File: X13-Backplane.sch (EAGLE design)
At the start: 24 parts, among them J1 284512-4, J2 284512-4, J3 284512-8, J4 284512-8, J5 284512-4, T1 284512-3, T2 284512-3, T3 284512-3, T4 284512-3, T5 284512-3, T6 284512-3, T7 284512-3, T8 284512-3

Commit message: updated schematic
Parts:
- removed R2: 10k, SparkFun-Resistors:10KOHM-0603-1/10W-1%
- removed R3: 4.7k, SparkFun-Resistors:1KOHM-0603-1/10W-1%
- removed U$7, U$8: ESC2BACKPLANE, ESC_to_Backplane_Connectors:ESC2BACKPLANE
- added DIST_LOGIC_TO_BACKPLANE: IPL1-107-01-L-D-RE-P, Backplane_Dist_Logic_Connector:IPL1-107-01-L-D-RE-P
- added DIST_TO_BACKPLANE: (no value), Samtec MPPT Hermaphoditic 10 pos - MPPT-10-01-01-L-RA-SD:MPPT-10-01-01-L-RA-SD
- added J8: 284512-8, 284512-8:284512-8
- added R4: 22k, SparkFun-Resistors:26.7KOHM0603-1/10W-1%
- added R5: 4.7k, SparkFun-Resistors:1KOHM-0603-1/10W-1%
- added SOLENOID_CONNECTOR: SAMTEC-CLT-111-01-X-DJ, Solenoid Connector - SAMTEC-CLT-111-01-X-D:SAMTEC-CLT-111-01-X-DJ
- added U$1, U$2: BACKPLANE_CONNECTORS, BLHeli_32 45A:BACKPLANE_CONNECTORS
- R1: value 22k -> 10k; device SparkFun-Resistors:26.7KOHM0603-1/10W-1% -> SparkFun-Resistors:10KOHM-0603-1/10W-1%
- U$3: value ESC2BACKPLANE -> BACKPLANE_CONNECTORS; device ESC_to_Backplane_Connectors:ESC2BACKPLANE -> BLHeli_32 45A:BACKPLANE_CONNECTORS
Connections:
- removed net ESC-ID_1: R1.2, U$3G$1.P$8
- removed net ESC-ID_2: R2.2, U$7G$1.P$8
- removed net ESC-ID_3: R3.2, U$8G$1.P$8
- new net ALERT_1: DIST_LOGIC_TO_BACKPLANE.11, SOLENOID_CONNECTOR.18
- new net ALERT_2: DIST_LOGIC_TO_BACKPLANE.10, SOLENOID_CONNECTOR.17
- new net C2_1: DIST_LOGIC_TO_BACKPLANE.8, SOLENOID_CONNECTOR.16
- new net C2_2: DIST_LOGIC_TO_BACKPLANE.7, SOLENOID_CONNECTOR.15
- new net CLK: DIST_LOGIC_TO_BACKPLANE.9, SOLENOID_CONNECTOR.20
- new net DATA: DIST_LOGIC_TO_BACKPLANE.12, SOLENOID_CONNECTOR.22
- new net ESCID_1: R4.2, U$1G$3.12
- new net ESCID_2: R1.2, U$2G$3.12
- new net ESCID_3: R5.2, U$3G$3.12
- new net SOL1_1: J8.1, SOLENOID_CONNECTOR.2
- new net SOL2_1: J8.2, SOLENOID_CONNECTOR.1
- new net SOL3_1: J8.3, SOLENOID_CONNECTOR.3
- new net SOL4_1: J8.4, SOLENOID_CONNECTOR.5
- new net SOL5_1: J8.5, SOLENOID_CONNECTOR.7
- new net SOL6_1: J8.6, SOLENOID_CONNECTOR.9
- net 12V: now also DIST_TO_BACKPLANE.10, DIST_TO_BACKPLANE.6, DIST_TO_BACKPLANE.7, DIST_TO_BACKPLANE.8, DIST_TO_BACKPLANE.9, SOLENOID_CONNECTOR.11, U$1G$1.1, U$1G$1.2, U$1G$1.3, U$1G$1.4, U$1G$1.5, U$1G$1.6, U$1G$1.7, U$1G$1.8, U$1G$2.1, U$1G$2.2, U$1G$2.3, U$1G$2.4, U$1G$2.5, U$1G$2.6, U$1G$2.7, U$1G$2.8, U$2G$1.1, U$2G$1.2, U$2G$1.3, U$2G$1.4, U$2G$1.5, U$2G$1.6, U$2G$1.7, U$2G$1.8, U$2G$2.1, U$2G$2.2, U$2G$2.3, U$2G$2.4, U$2G$2.5, U$2G$2.6, U$2G$2.7, U$2G$2.8, U$3G$1.1, U$3G$1.2, U$3G$1.3, U$3G$1.4, U$3G$1.5, U$3G$1.6, U$3G$1.7, U$3G$1.8, U$3G$2.1, U$3G$2.2, U$3G$2.3, U$3G$2.4, U$3G$2.5, U$3G$2.6, U$3G$2.7, U$3G$2.8; no longer U$3G$1.P$10, U$3G$1.P$11, U$3G$1.P$12, U$3G$1.P$13, U$3G$1.P$23, U$3G$1.P$24, U$3G$1.P$25, U$3G$1.P$26, U$3G$1.P$27, U$3G$1.P$9, U$3G$2.P$A, U$3G$2.P$B, U$3G$2.P$C, U$3G$2.P$D, U$3G$2.P$E, U$3G$2.P$O, U$3G$2.P$P, U$3G$2.P$Q, U$3G$2.P$R, U$3G$2.P$S, U$7G$1.P$10, U$7G$1.P$11, U$7G$1.P$12, U$7G$1.P$13, U$7G$1.P$23, U$7G$1.P$24, U$7G$1.P$25, U$7G$1.P$26, U$7G$1.P$27, U$7G$1.P$9, U$7G$2.P$A, U$7G$2.P$B, U$7G$2.P$C, U$7G$2.P$D, U$7G$2.P$E, U$7G$2.P$O, U$7G$2.P$P, U$7G$2.P$Q, U$7G$2.P$R, U$7G$2.P$S, U$8G$1.P$10, U$8G$1.P$11, U$8G$1.P$12, U$8G$1.P$13, U$8G$1.P$23, U$8G$1.P$24, U$8G$1.P$25, U$8G$1.P$26, U$8G$1.P$27, U$8G$1.P$9, U$8G$2.P$A, U$8G$2.P$B, U$8G$2.P$C, U$8G$2.P$D, U$8G$2.P$E, U$8G$2.P$O, U$8G$2.P$P, U$8G$2.P$Q, U$8G$2.P$R, U$8G$2.P$S
- net 3.3V: now also DIST_LOGIC_TO_BACKPLANE.4, SOLENOID_CONNECTOR.6, U$1G$3.1, U$1G$3.2, U$1G$3.3, U$1G$3.4, U$2G$3.1, U$2G$3.2, U$2G$3.3, U$2G$3.4, U$3G$3.1, U$3G$3.2, U$3G$3.3, U$3G$3.4; no longer U$3G$2.P$G, U$3G$2.P$H, U$3G$2.P$U, U$3G$2.P$V, U$7G$2.P$G, U$7G$2.P$H, U$7G$2.P$U, U$7G$2.P$V, U$8G$2.P$G, U$8G$2.P$H, U$8G$2.P$U, U$8G$2.P$V
- net 5V: now also DIST_LOGIC_TO_BACKPLANE.1, DIST_LOGIC_TO_BACKPLANE.2, DIST_LOGIC_TO_BACKPLANE.3
- net CAN_H: now also SOLENOID_CONNECTOR.19, U$1G$3.5, U$2G$3.5, U$3G$3.5; no longer U$3G$1.P$6, U$7G$1.P$6, U$8G$1.P$6
- net CAN_L: now also SOLENOID_CONNECTOR.21, U$1G$3.7, U$2G$3.7, U$3G$3.7; no longer U$3G$1.P$7, U$7G$1.P$7, U$8G$1.P$7
- net GND: now also DIST_LOGIC_TO_BACKPLANE.5, DIST_LOGIC_TO_BACKPLANE.6, DIST_TO_BACKPLANE.1, DIST_TO_BACKPLANE.2, DIST_TO_BACKPLANE.3, DIST_TO_BACKPLANE.4, DIST_TO_BACKPLANE.5, R4.1, R5.1, SOLENOID_CONNECTOR.10, SOLENOID_CONNECTOR.12, SOLENOID_CONNECTOR.4, SOLENOID_CONNECTOR.8, U$1G$1.10, U$1G$1.11, U$1G$1.12, U$1G$1.9, U$1G$2.10, U$1G$2.11, U$1G$2.12, U$1G$2.9, U$2G$1.10, U$2G$1.11, U$2G$1.12, U$2G$1.9, U$2G$2.10, U$2G$2.11, U$2G$2.12, U$2G$2.9, U$3G$1.10, U$3G$1.11, U$3G$1.12, U$3G$1.9, U$3G$2.10, U$3G$2.11, U$3G$2.12, U$3G$2.9; no longer R2.1, R3.1, U$3G$1.P$1, U$3G$1.P$15, U$3G$1.P$16, U$3G$1.P$17, U$3G$1.P$18, U$3G$1.P$2, U$3G$1.P$3, U$3G$1.P$4, U$3G$2.P$AA, U$3G$2.P$BB, U$3G$2.P$J, U$3G$2.P$K, U$3G$2.P$L, U$3G$2.P$M, U$3G$2.P$N, U$3G$2.P$X, U$3G$2.P$Y, U$3G$2.P$Z, U$7G$1.P$1, U$7G$1.P$15, U$7G$1.P$16, U$7G$1.P$17, U$7G$1.P$18, U$7G$1.P$2, U$7G$1.P$3, U$7G$1.P$4, U$7G$2.P$AA, U$7G$2.P$BB, U$7G$2.P$J, U$7G$2.P$K, U$7G$2.P$L, U$7G$2.P$M, U$7G$2.P$N, U$7G$2.P$X, U$7G$2.P$Y, U$7G$2.P$Z, U$8G$1.P$1, U$8G$1.P$15, U$8G$1.P$16, U$8G$1.P$17, U$8G$1.P$18, U$8G$1.P$2, U$8G$1.P$3, U$8G$1.P$4, U$8G$2.P$AA, U$8G$2.P$BB, U$8G$2.P$J, U$8G$2.P$K, U$8G$2.P$L, U$8G$2.P$M, U$8G$2.P$N, U$8G$2.P$X, U$8G$2.P$Y, U$8G$2.P$Z
- net NRST: now also U$1G$3.6, U$2G$3.6, U$3G$3.6; no longer U$3G$1.P$20, U$7G$1.P$20, U$8G$1.P$20
- net PROG_1: now also U$1G$3.8; no longer U$3G$1.P$5
- net PROG_2: now also U$2G$3.8; no longer U$7G$1.P$5
- net PROG_3: now also U$3G$3.8; no longer U$8G$1.P$5
- net SWCLK_1: now also U$1G$3.11; no longer U$3G$1.P$22
- net SWCLK_2: now also U$2G$3.11; no longer U$7G$1.P$22
- net SWCLK_3: now also U$3G$3.11; no longer U$8G$1.P$22
- net SWDIO_1: now also U$1G$3.9; no longer U$3G$1.P$21
- net SWDIO_2: now also U$2G$3.9; no longer U$7G$1.P$21
- net SWDIO_3: now also U$3G$3.9; no longer U$8G$1.P$21
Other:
- note added: "Solenoid"
- moved on the sheet: MUX, R1

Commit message: wired board
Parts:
- added C1, C2, C3: 10nF, SparkFun-Capacitors:10NF-0603-50V-10%
- added H1, H2, H3: 6-32-HOLE, Mounting Holes:6-32-HOLE
- added J6: 284512-4, 284512-4:284512-4
- added R2, R3, R6: 10k, SparkFun-Resistors:10KOHM-0603-1/10W-1%
- J1, J5: value 284512-4 -> PXC-PTSM-04-RA-1778641; device 284512-4:284512-4 -> Phoenix Contact PTSM-04-V-1778573:PXC-PTSM-04-RA-1778641
- J4: value 284512-8 -> PXC-PTSM-04-RA-1778641; device 284512-8:284512-8 -> Phoenix Contact PTSM-04-V-1778573:PXC-PTSM-04-RA-1778641
- SOLENOID_CONNECTOR: value SAMTEC-CLT-111-01-X-DJ -> TMM-111-01-T-D; device Solenoid Connector - SAMTEC-CLT-111-01-X-D:SAMTEC-CLT-111-01-X-DJ -> Samtec low profile male headers - TMM-111-01-T-D:TMM-111-01-T-D
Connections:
- new net SHIELD_1: C1.1, J1.4, R2.2
- new net SHIELD_2: C2.1, J4.4, R3.2
- new net SHIELD_3: C3.1, J5.4, R6.2
- net 12V: no longer J5.1, J5.2
- net 5V: now also J5.1, J5.2, J6.1; no longer J4.3
- net CAN_H: now also J6.2; no longer J4.4
- net CAN_L: now also J6.3; no longer J4.5
- net GND: now also C1.2, C2.2, C3.2, J4.3, J6.4, J8.7, J8.8, R2.1, R3.1, R6.1; no longer J1.4, J4.6, J4.7, J4.8, J5.4
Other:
- note removed: "Fan"
- moved on the sheet: J1, J2, J5

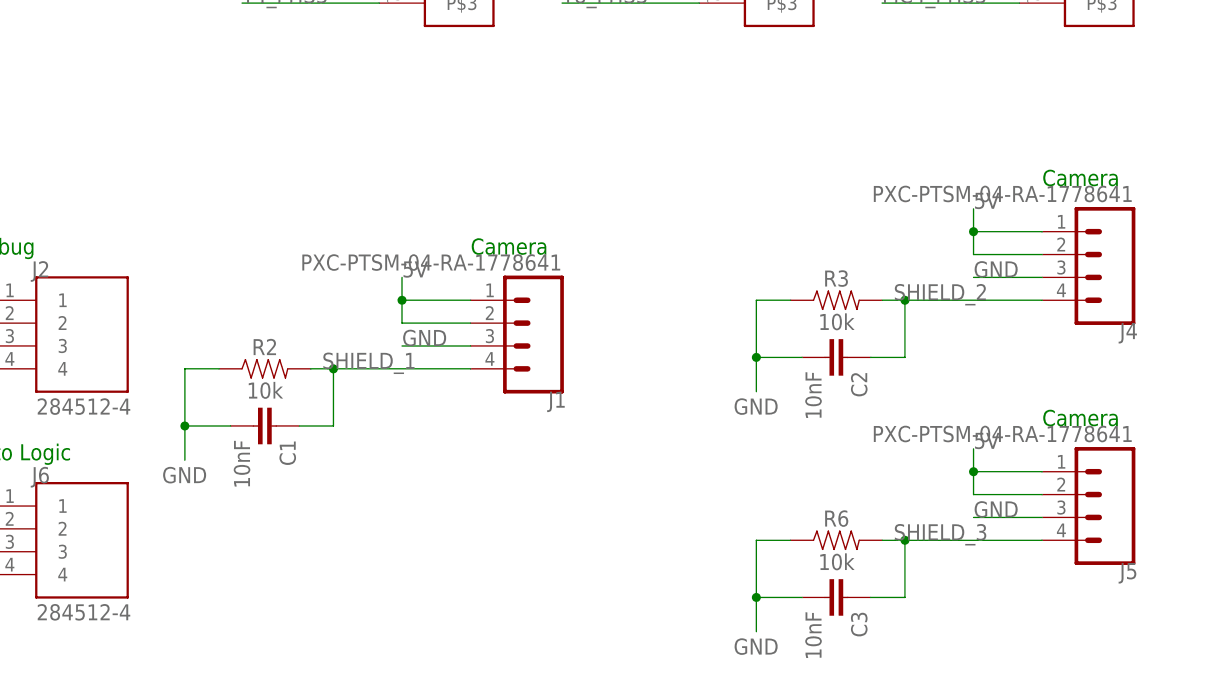
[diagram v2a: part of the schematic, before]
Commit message: updated solenoid connector
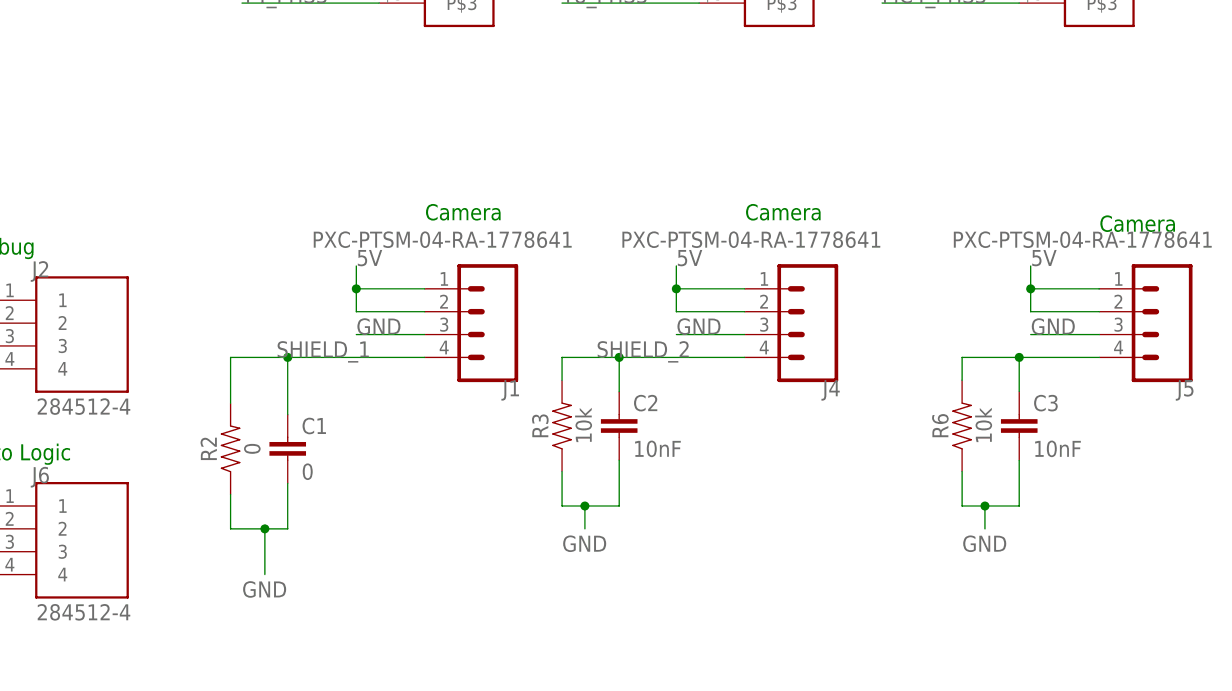
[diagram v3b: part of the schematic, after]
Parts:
- C1: value 10nF -> 0
- R2: value 10k -> 0
- SOLENOID_CONNECTOR: value TMM-111-01-T-D -> BKP-TO-SOL; device Samtec low profile male headers - TMM-111-01-T-D:TMM-111-01-T-D -> Solenoid Connector (backplane side):BKP-TO-SOL
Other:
- moved on the sheet: C1, C2, C3, J1, J4, J5, R2, R3, R6

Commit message: updated mux
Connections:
- removed net SWCLK_4: MUX.1Y3
- removed net SWDIO_4: MUX.2Y3
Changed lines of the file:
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@@
 <setting verticaltext="up"/>
 </settings>
-<grid distance="0.05" unitdist="inch" unit="inch" style="lines" multiple="1" display="no" altdistance="0.01" altunitdist="inch" altunit="inch"/>
+<grid distance="0.1" unitdist="inch" unit="inch" style="lines" multiple="1" display="no" altdistance="0.01" altunitdist="inch" altunit="inch"/>
 <layers>
 <layer number="1" name="Top" color="4" fill="1" visible="no" active="no"/>
@@
 </segment>
 </net>
-<net name="SWDIO_4" class="0">
-<segment>
-<pinref part="MUX" gate="G$1" pin="2Y3"/>
-<wire x1="-96.52" y1="77.47" x2="-106.68" y2="77.47" width="0.1524" layer="91"/>
-<label x="-106.68" y="77.47" size="1.778" layer="95"/>
-</segment>
-</net>
-<net name="SWCLK_4" class="0">
-<segment>
-<pinref part="MUX" gate="G$1" pin="1Y3"/>
-<wire x1="-68.58" y1="72.39" x2="-58.42" y2="72.39" width="0.1524" layer="91"/>
-<label x="-68.58" y="72.39" size="1.778" layer="95"/>
-</segment>
-</net>

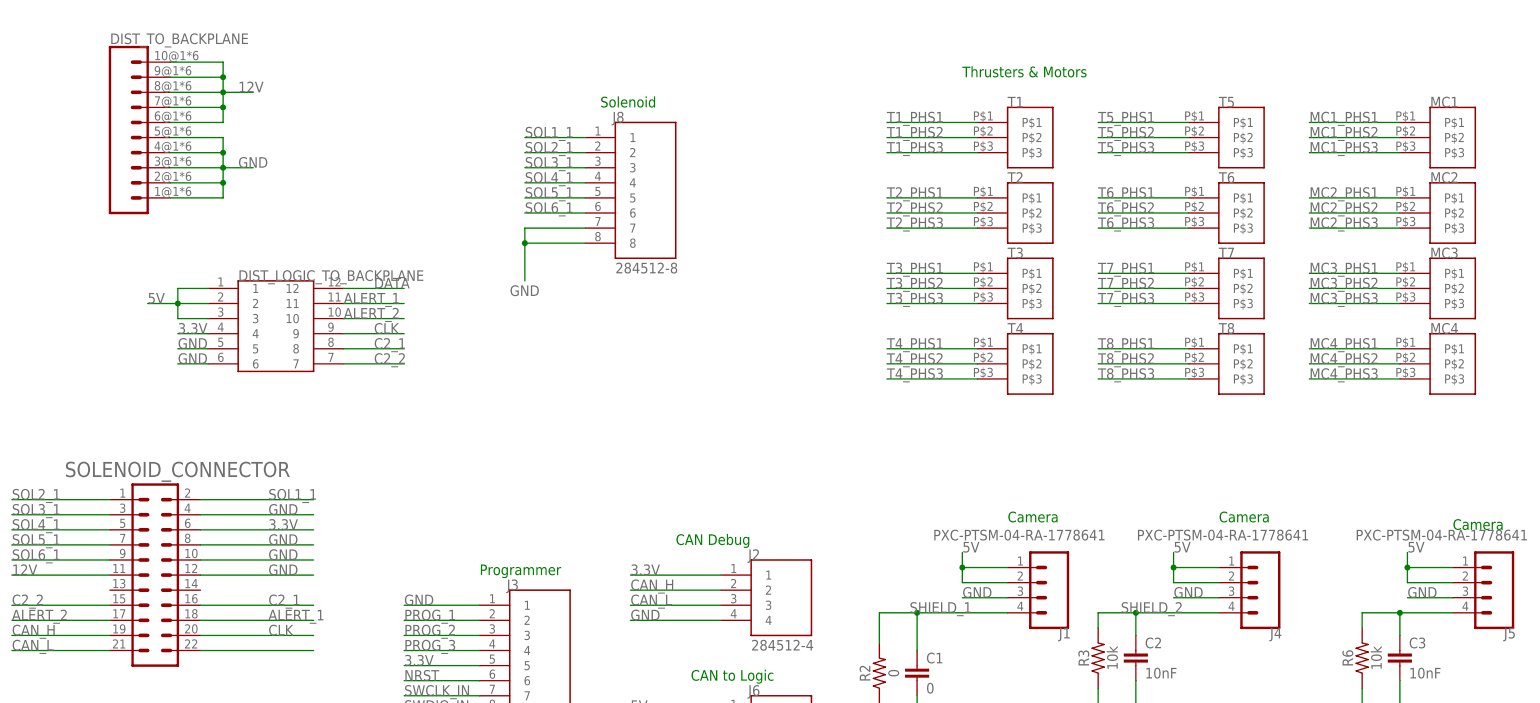
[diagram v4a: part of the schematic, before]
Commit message: Placed Solenoid Connector and schematic pinout
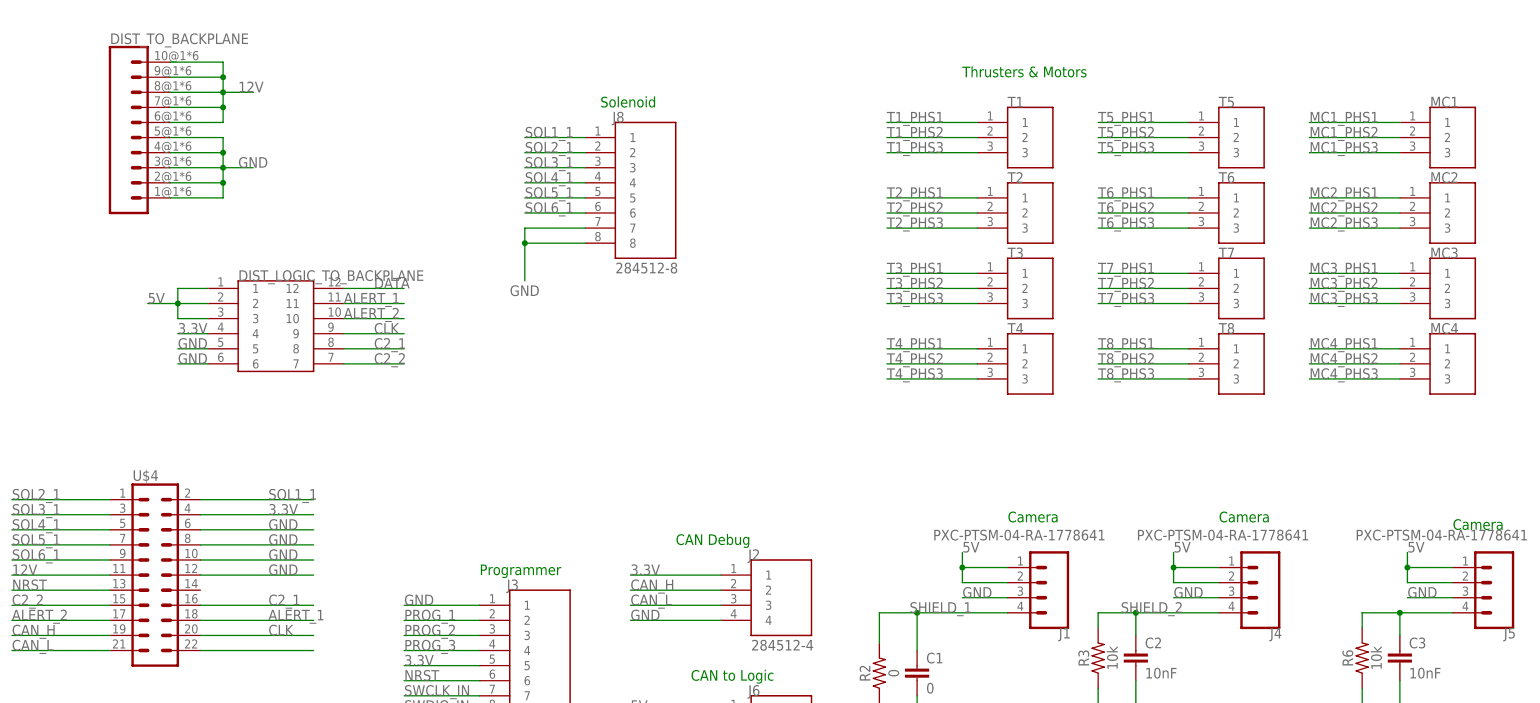
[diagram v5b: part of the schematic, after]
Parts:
- renumbered SOLENOID_CONNECTOR to U$4
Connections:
- new net DATA1: U$4.22
- net 3.3V: now also U$4.4; no longer U$4.6
- net DATA: no longer U$4.22
- net GND: now also U$4.6; no longer U$4.4
- net MC1_PHS1: now also MC1.1; no longer MC1.P$1
- net MC1_PHS2: now also MC1.2; no longer MC1.P$2
- net MC1_PHS3: now also MC1.3; no longer MC1.P$3
- net MC2_PHS1: now also MC2.1; no longer MC2.P$1
- net MC2_PHS2: now also MC2.2; no longer MC2.P$2
- net MC2_PHS3: now also MC2.3; no longer MC2.P$3
- net MC3_PHS1: now also MC3.1; no longer MC3.P$1
- net MC3_PHS2: now also MC3.2; no longer MC3.P$2
- net MC3_PHS3: now also MC3.3; no longer MC3.P$3
- net MC4_PHS1: now also MC4.1; no longer MC4.P$1
- net MC4_PHS2: now also MC4.2; no longer MC4.P$2
- net MC4_PHS3: now also MC4.3; no longer MC4.P$3
- net NRST: now also U$4.13
- net T1_PHS1: now also T1.1; no longer T1.P$1
- net T1_PHS2: now also T1.2; no longer T1.P$2
- net T1_PHS3: now also T1.3; no longer T1.P$3
- net T2_PHS1: now also T2.1; no longer T2.P$1
- net T2_PHS2: now also T2.2; no longer T2.P$2
- net T2_PHS3: now also T2.3; no longer T2.P$3
- net T3_PHS1: now also T3.1; no longer T3.P$1
- net T3_PHS2: now also T3.2; no longer T3.P$2
- net T3_PHS3: now also T3.3; no longer T3.P$3
- net T4_PHS1: now also T4.1; no longer T4.P$1
- net T4_PHS2: now also T4.2; no longer T4.P$2
- net T4_PHS3: now also T4.3; no longer T4.P$3
- net T5_PHS1: now also T5.1; no longer T5.P$1
- net T5_PHS2: now also T5.2; no longer T5.P$2
- net T5_PHS3: now also T5.3; no longer T5.P$3
- net T6_PHS1: now also T6.1; no longer T6.P$1
- net T6_PHS2: now also T6.2; no longer T6.P$2
- net T6_PHS3: now also T6.3; no longer T6.P$3
- net T7_PHS1: now also T7.1; no longer T7.P$1
- net T7_PHS2: now also T7.2; no longer T7.P$2
- net T7_PHS3: now also T7.3; no longer T7.P$3
- net T8_PHS1: now also T8.1; no longer T8.P$1
- net T8_PHS2: now also T8.2; no longer T8.P$2
- net T8_PHS3: now also T8.3; no longer T8.P$3
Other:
- moved on the sheet: MC1, MC2, MC3, MC4, T1, T2, T3, T4, T5, T6, T7, T8
